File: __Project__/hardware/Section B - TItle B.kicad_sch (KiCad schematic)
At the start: 0 parts

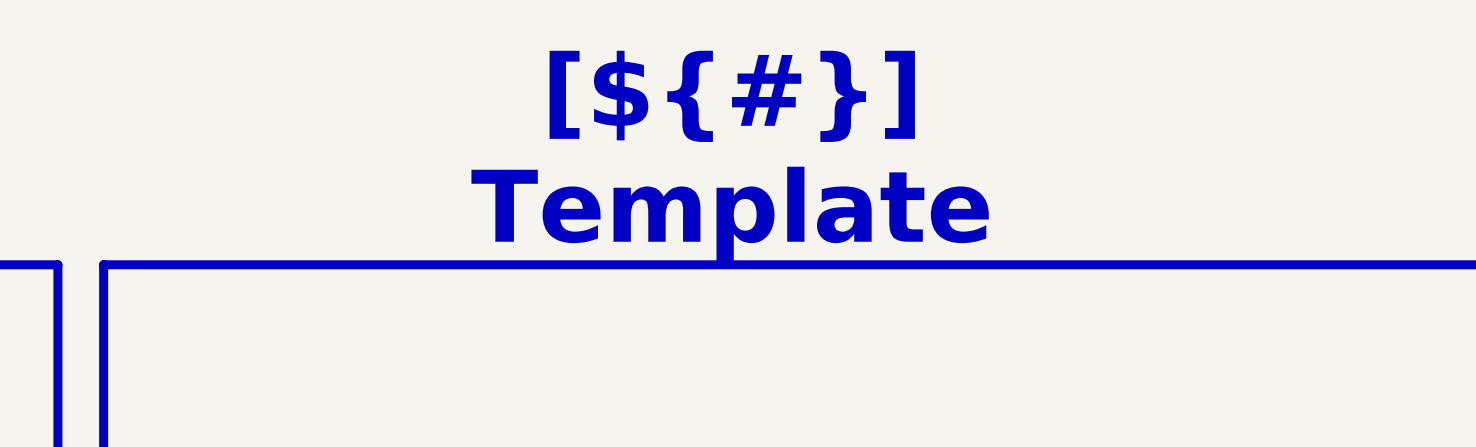
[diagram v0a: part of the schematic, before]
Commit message: Fix JST footprints
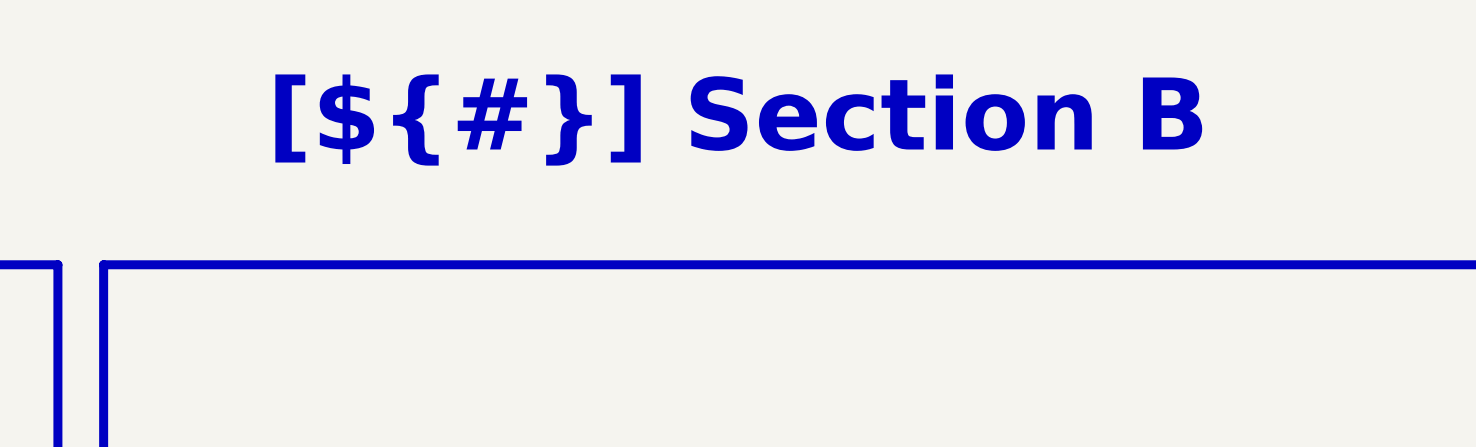
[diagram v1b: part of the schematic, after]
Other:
- title: Template -> Section B
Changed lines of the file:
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@@
 	(paper "A3")
 	(title_block
-		(title "Template")
+		(title "Section B")
 		(date "2025-06-05")
 		(rev "${REVISION}")
@@
 		)
 	)
+	(text_box "[${#}] ${TITLE}"
+		(exclude_from_sim no)
+		(at 12.7 12.7 0)
+		(size 394.97 20.32)
+		(margins 5.9999 5.9999 5.9999 5.9999)
+		(stroke
+			(width -0.0001)
+			(type default)
+		)
+		(fill
+			(type none)
+		)
+		(effects
+			(font
+				(face "Times New Roman")
+				(size 8 8)
+				(thickness 1.2)
+				(bold yes)
+				(color 162 22 34 1)
+			)
+		)
+	)
 	(text_box "Block Description"
 		(exclude_from_sim no)
@@
 		)
 	)
-	(text_box "[${#}] ${TITLE}"
-		(exclude_from_sim no)
-		(at 161.29 20.32 0)
-		(size 96.52 12.7)
-		(margins 5.9999 5.9999 5.9999 5.9999)
-		(stroke
-			(width -0.0001)
-			(type default)
-		)
-		(fill
-			(type none)
-		)
-		(effects
-			(font
-				(face "Times New Roman")
-				(size 8 8)
-				(thickness 1.2)
-				(bold yes)
-				(color 162 22 34 1)
-			)
-		)
-	)
